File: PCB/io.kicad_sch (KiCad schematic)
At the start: 6 parts

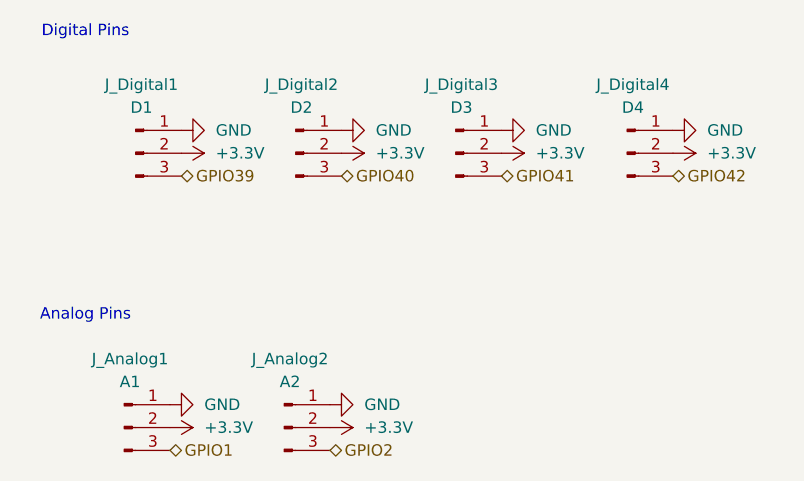
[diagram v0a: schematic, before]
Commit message: refactor: Update PCB with power jumper
This adds a jumper to connect the digital and analog pins to either 3.3v or 5v depending on the jumper position.
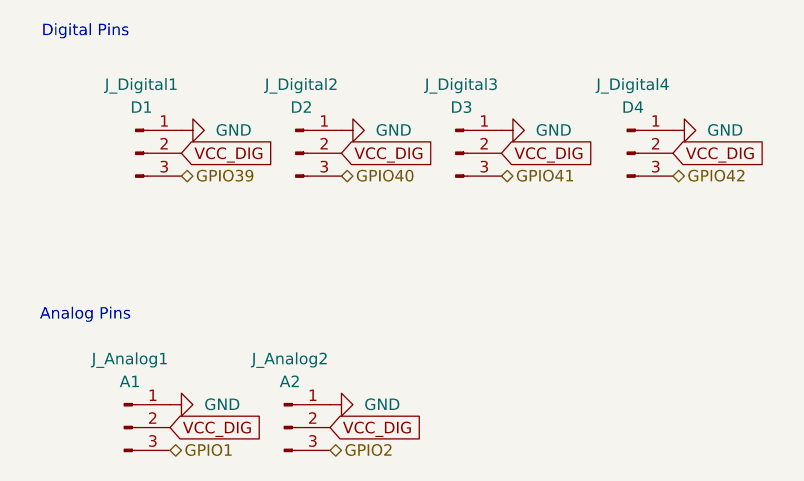
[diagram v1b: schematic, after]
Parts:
- J_Analog1, J_Analog2, J_Digital1, J_Digital2, J_Digital3, J_Digital4: now left out of the parts list
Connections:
- net +3.3V renamed VCC_DIG
